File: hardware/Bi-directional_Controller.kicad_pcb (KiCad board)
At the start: 2 copper layers, 70.5 x 45.5 mm, 58 parts, among them J1 ON/OFF, J13 MOTOR, J14 Serial, J2 Conn_01x06, J3 Conn_02x03_Odd_Even, J7 BAT 12V-18V, J8 CH1, Q1 BSS138, Q10 AOD240, Q12 AO6401A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

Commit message: symbols update
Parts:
- C11: value 100u -> 100u/35V
- C12: value 1000u -> 1000u/10V
- J7: value BAT 12V-18V -> BAT 12V
- R10: value 22k -> 22k*
- SW1: value SW_Push -> RESET
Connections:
- net Net-(R1-Pad1) renamed CH1
- net Net-(R17-Pad2) renamed DIR_R
- net Net-(R20-Pad2) renamed DIR_L
- net Net-(R22-Pad1) renamed PULS_L
- net Net-(R23-Pad1) renamed PULS_R

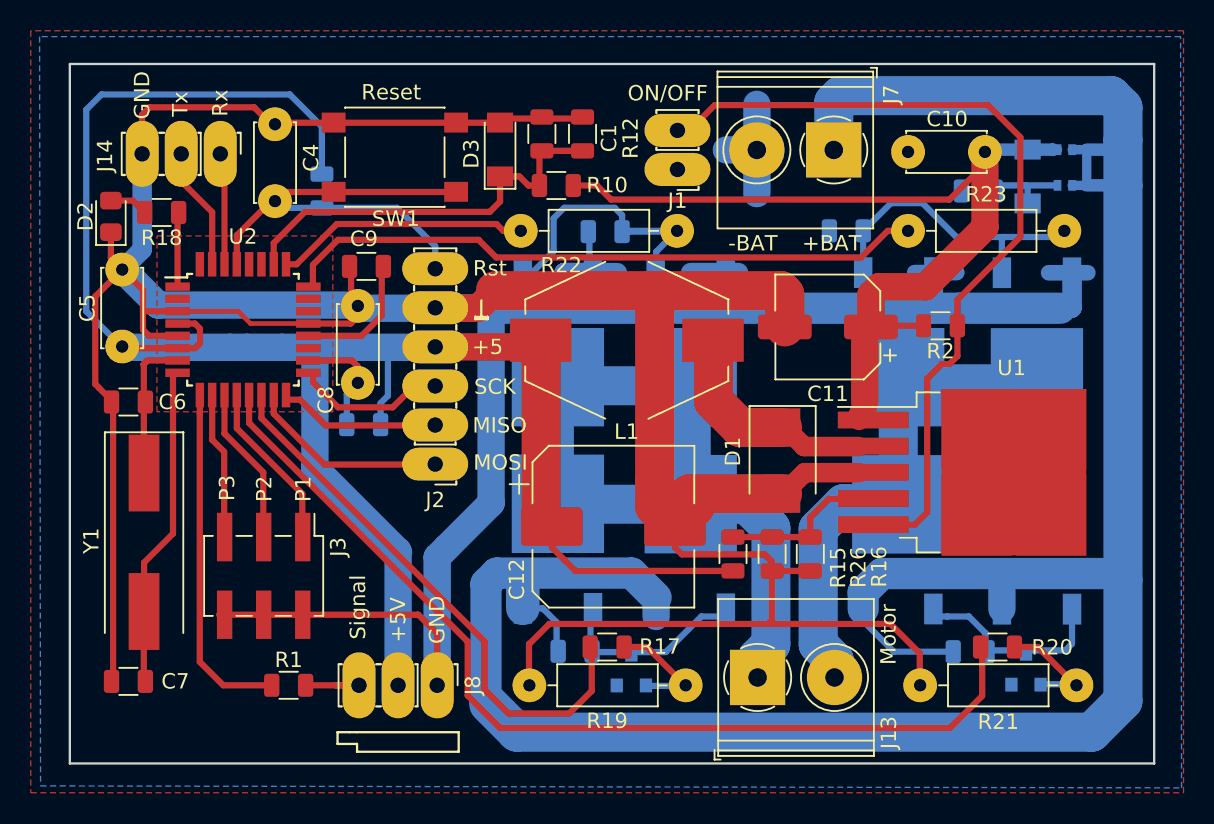
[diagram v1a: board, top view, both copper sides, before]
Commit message: symbol update
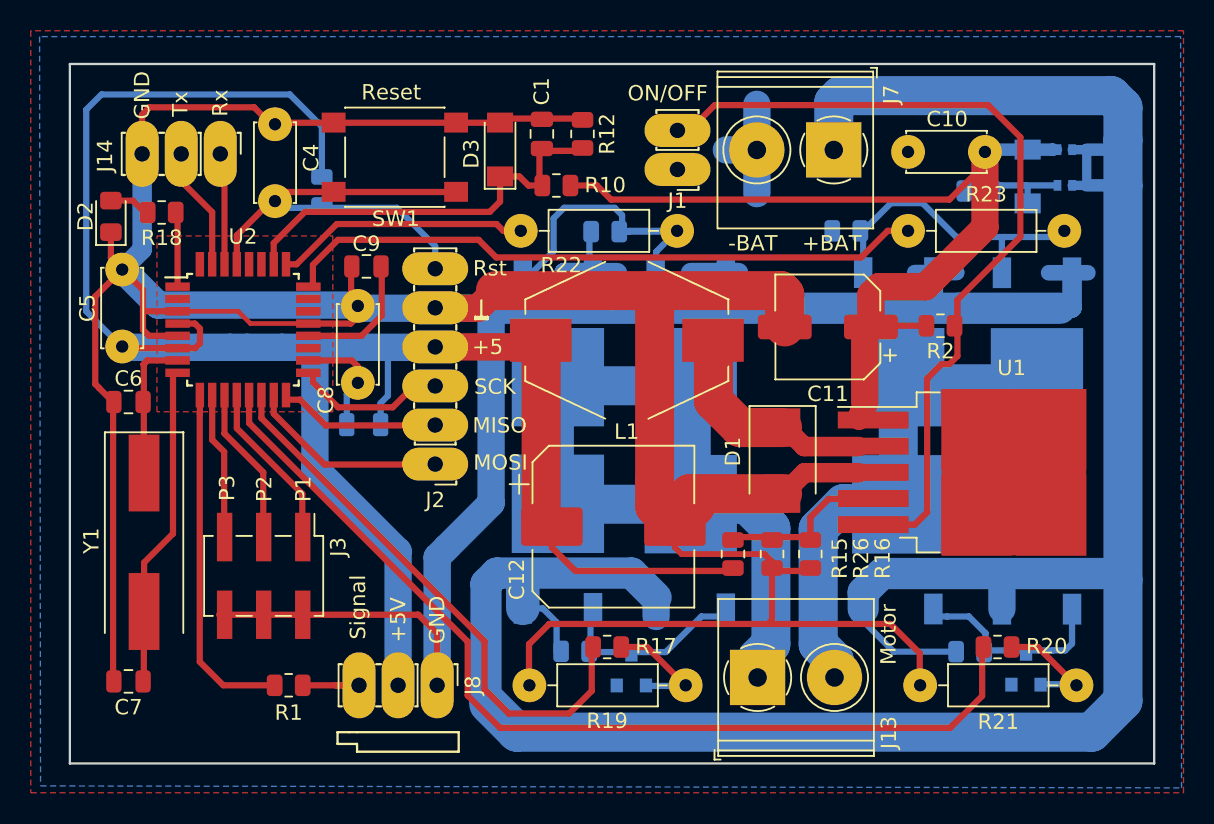
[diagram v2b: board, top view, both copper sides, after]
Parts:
- C1, C6, C7, C9: footprint obbo_footprints:C_0805K -> Capacitor_SMD:C_0805_2012Metric
- R1, R10, R11, R12, R13, R14, R15, R17, R18, R2, R20, R24, R25, R3: footprint obbo_footprints:R_0805K -> Resistor_SMD:R_0805_2012Metric
- R16: value 100k* -> 11k*; footprint obbo_footprints:R_0805K -> Resistor_SMD:R_0805_2012Metric
- R26: value 3k3 -> 4k7; footprint obbo_footprints:R_0805K -> Resistor_SMD:R_0805_2012Metric
- U2: footprint Housings_QFP:TQFP-32_7x7mm_Pitch0.8mm -> Package_QFP:TQFP-32_7x7mm_P0.8mm
